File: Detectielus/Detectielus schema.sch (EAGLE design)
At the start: 12 parts, among them IC1 74HC132D, X1 Arduino

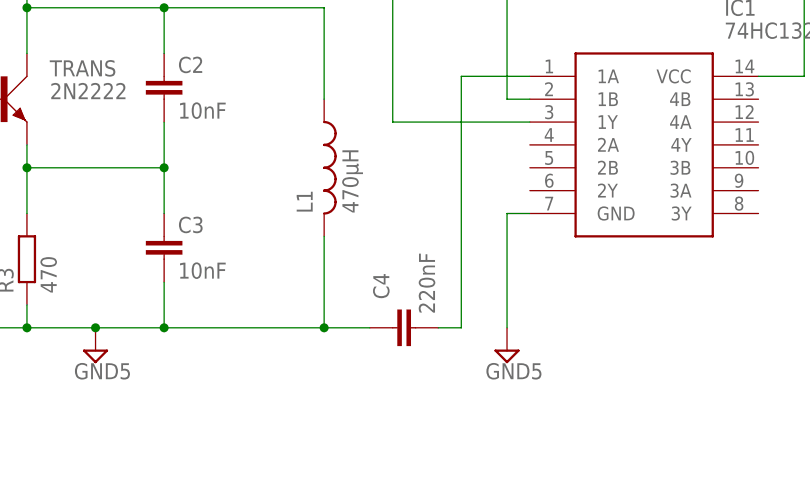
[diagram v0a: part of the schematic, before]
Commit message: Aanpassing schema (diode)
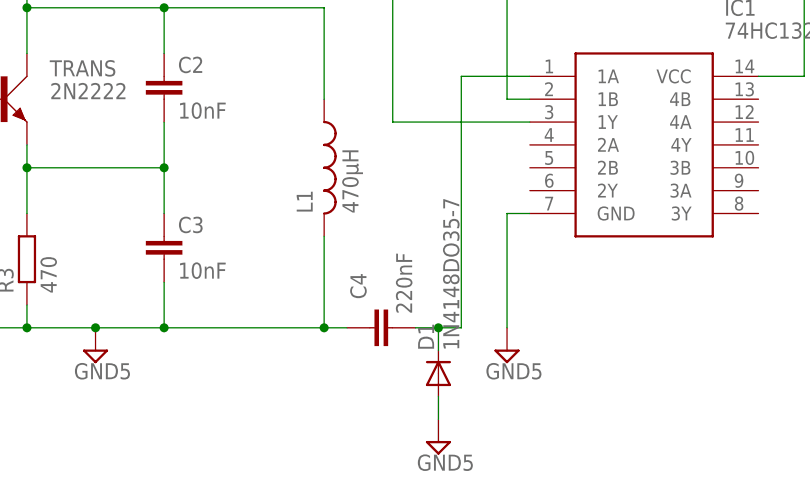
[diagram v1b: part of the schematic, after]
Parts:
- added D1: 1N4148DO35-7, Detectielus library:1N4148DO35-7
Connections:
- net GND5: now also D1.A
- net N$1: now also D1.C
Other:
- moved on the sheet: C4
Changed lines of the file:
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@@
 <layer number="97" name="Info" color="7" fill="1" visible="yes" active="yes"/>
 <layer number="98" name="Guide" color="6" fill="1" visible="yes" active="yes"/>
+<layer number="99" name="SpiceOrder" color="5" fill="1" visible="yes" active="yes"/>
 </layers>
 <schematic xreflabel="%F%N/%S.%C%R" xrefpart="/%S.%C%R">
@@
 <part name="SUPPLY4" library="Detectielus library" deviceset="GND5" device=""/>
 <part name="X1" library="Detectielus library" deviceset="332-02" device="" package3d_urn="urn:adsk.eagle:package:6810/1" value="Arduino"/>
+<part name="SUPPLY5" library="Detectielus library" deviceset="GND5" device=""/>
+<part name="D1" library="Detectielus library" deviceset="1N4148" device="DO35-7" package3d_urn="urn:adsk.eagle:package:43339/1"/>
 </parts>
 <sheets>
@@
 <attribute name="VALUE" x="16.764" y="28.321" size="1.778" layer="96"/>
 </instance>
-<instance part="C4" gate="G$1" x="40.64" y="22.86" smashed="yes" rot="R90">
-<attribute name="NAME" x="38.481" y="28.956" size="1.778" layer="95" rot="R270"/>
-<attribute name="VALUE" x="45.339" y="24.384" size="1.778" layer="96" rot="R90"/>
+<instance part="C4" gate="G$1" x="38.1" y="22.86" smashed="yes" rot="R90">
+<attribute name="NAME" x="35.941" y="28.956" size="1.778" layer="95" rot="R270"/>
+<attribute name="VALUE" x="42.799" y="24.384" size="1.778" layer="96" rot="R90"/>
 </instance>
 <instance part="L1" gate="G$1" x="33.02" y="40.64" smashed="yes">
@@
 <attribute name="NAME" x="41.402" y="73.66" size="1.524" layer="95" rot="R90"/>
 <attribute name="VALUE" x="39.243" y="70.358" size="1.778" layer="96" rot="R90"/>
+</instance>
+<instance part="SUPPLY5" gate="G$1" x="45.72" y="10.16" smashed="yes">
+<attribute name="VALUE" x="43.307" y="6.985" size="1.778" layer="96"/>
+</instance>
+<instance part="D1" gate="G$1" x="45.72" y="17.78" smashed="yes" rot="R90">
+<attribute name="NAME" x="45.2374" y="20.32" size="1.778" layer="95" rot="R90"/>
+<attribute name="VALUE" x="48.0314" y="20.32" size="1.778" layer="96" rot="R90"/>
 </instance>
 </instances>
@@
 <segment>
 <pinref part="C4" gate="G$1" pin="2"/>
+<wire x1="43.18" y1="22.86" x2="45.72" y2="22.86" width="0.1524" layer="91"/>
+<pinref part="IC1" gate="G$1" pin="1A"/>
 <wire x1="45.72" y1="22.86" x2="48.26" y2="22.86" width="0.1524" layer="91"/>
-<pinref part="IC1" gate="G$1" pin="1A"/>
 <wire x1="48.26" y1="22.86" x2="48.26" y2="50.8" width="0.1524" layer="91"/>
 <wire x1="48.26" y1="50.8" x2="55.88" y2="50.8" width="0.1524" layer="91"/>
+<wire x1="45.72" y1="20.32" x2="45.72" y2="22.86" width="0.1524" layer="91"/>
+<junction x="45.72" y="22.86"/>
+<pinref part="D1" gate="G$1" pin="C"/>
 </segment>
 </net>
@@
 <junction x="15.24" y="22.86"/>
 <pinref part="C4" gate="G$1" pin="1"/>
-<wire x1="38.1" y1="22.86" x2="33.02" y2="22.86" width="0.1524" layer="91"/>
+<wire x1="35.56" y1="22.86" x2="33.02" y2="22.86" width="0.1524" layer="91"/>
 <junction x="33.02" y="22.86"/>
 <pinref part="SUPPLY4" gate="G$1" pin="GND5"/>
@@
 <junction x="-15.24" y="22.86"/>
 </segment>
-</net>
+<segment>
+<pinref part="SUPPLY5" gate="G$1" pin="GND5"/>
+<wire x1="45.72" y1="12.7" x2="45.72" y2="15.24" width="0.1524" layer="91"/>
+<pinref part="D1" gate="G$1" pin="A"/>
+</segment>
+</net>

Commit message: Schema's en logboek
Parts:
- added X2, X3: (no value), Detectielus library:90-2
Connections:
- removed net VCC: IC1.1B, IC1.VCC, R1.2, R2.2
- new net GND: X2.1, X3.1
- new net VCC-24V: R1.2, R2.2, X2.2
- new net VCC-5V: IC1.1B, IC1.VCC, X3.2
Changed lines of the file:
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@@
 <setting verticaltext="up"/>
 </settings>
-<grid distance="0.1" unitdist="inch" unit="inch" style="lines" multiple="1" display="yes" altdistance="0.01" altunitdist="inch" altunit="inch"/>
+<grid distance="0.1" unitdist="inch" unit="inch" style="lines" multiple="1" display="no" altdistance="0.01" altunitdist="inch" altunit="inch"/>
 <layers>
 <layer number="1" name="Top" color="4" fill="1" visible="no" active="no"/>
@@
 <part name="SUPPLY3" library="Detectielus library" deviceset="GND5" device=""/>
 <part name="SUPPLY4" library="Detectielus library" deviceset="GND5" device=""/>
+<part name="D1" library="Detectielus library" deviceset="1N4148" device="DO35-7" package3d_urn="urn:adsk.eagle:package:43339/1"/>
 <part name="X1" library="Detectielus library" deviceset="332-02" device="" package3d_urn="urn:adsk.eagle:package:6810/1" value="Arduino"/>
 <part name="SUPPLY5" library="Detectielus library" deviceset="GND5" device=""/>
-<part name="D1" library="Detectielus library" deviceset="1N4148" device="DO35-7" package3d_urn="urn:adsk.eagle:package:43339/1"/>
+<part name="X2" library="Detectielus library" deviceset="90-2" device="" package3d_urn="urn:adsk.eagle:package:11443/1"/>
+<part name="X3" library="Detectielus library" deviceset="90-2" device="" package3d_urn="urn:adsk.eagle:package:11443/1"/>
 </parts>
 <sheets>
@@
 <attribute name="VALUE" x="5.207" y="17.145" size="1.778" layer="96"/>
 </instance>
+<instance part="D1" gate="G$1" x="45.72" y="17.78" smashed="yes" rot="R90">
+<attribute name="NAME" x="45.2374" y="20.32" size="1.778" layer="95" rot="R90"/>
+<attribute name="VALUE" x="48.0314" y="20.32" size="1.778" layer="96" rot="R90"/>
+</instance>
 <instance part="X1" gate="-1" x="40.64" y="71.12" smashed="yes" rot="R90">
 <attribute name="NAME" x="41.402" y="73.66" size="1.524" layer="95" rot="R90"/>
@@
 <attribute name="VALUE" x="43.307" y="6.985" size="1.778" layer="96"/>
 </instance>
-<instance part="D1" gate="G$1" x="45.72" y="17.78" smashed="yes" rot="R90">
-<attribute name="NAME" x="45.2374" y="20.32" size="1.778" layer="95" rot="R90"/>
-<attribute name="VALUE" x="48.0314" y="20.32" size="1.778" layer="96" rot="R90"/>
+<instance part="X2" gate="G$1" x="-66.04" y="78.74" smashed="yes" rot="R180">
+<attribute name="NAME" x="-66.04" y="76.962" size="1.778" layer="95" rot="R180"/>
+<attribute name="VALUE" x="-66.04" y="84.582" size="1.778" layer="96" rot="R180"/>
+</instance>
+<instance part="X3" gate="G$1" x="-66.04" y="68.58" smashed="yes" rot="R180">
+<attribute name="NAME" x="-66.04" y="66.802" size="1.778" layer="95" rot="R180"/>
+<attribute name="VALUE" x="-66.04" y="74.422" size="1.778" layer="96" rot="R180"/>
 </instance>
 </instances>
@@
 </segment>
 </net>
-<net name="VCC" class="0">
-<segment>
-<pinref part="R1" gate="G$1" pin="2"/>
-<wire x1="-15.24" y1="71.12" x2="-15.24" y2="73.66" width="0.1524" layer="91"/>
-<wire x1="-15.24" y1="73.66" x2="-7.62" y2="73.66" width="0.1524" layer="91"/>
-<pinref part="SUPPLY1" gate="G$1" pin="VCC"/>
-<wire x1="-7.62" y1="73.66" x2="-7.62" y2="76.2" width="0.1524" layer="91"/>
-<pinref part="R2" gate="G$1" pin="2"/>
-<wire x1="0" y1="71.12" x2="0" y2="73.66" width="0.1524" layer="91"/>
-<wire x1="0" y1="73.66" x2="-7.62" y2="73.66" width="0.1524" layer="91"/>
-<junction x="-7.62" y="73.66"/>
-</segment>
+<net name="VCC-5V" class="0">
 <segment>
 <pinref part="IC1" gate="G$1" pin="1B"/>
@@
 <wire x1="86.36" y1="60.96" x2="53.34" y2="60.96" width="0.1524" layer="91"/>
 <junction x="53.34" y="60.96"/>
+<label x="63.5" y="60.96" size="1.778" layer="95"/>
+</segment>
+<segment>
+<pinref part="X3" gate="G$1" pin="2"/>
+<wire x1="-63.5" y1="71.12" x2="-60.96" y2="71.12" width="0.1524" layer="91"/>
+<label x="-63.246" y="71.374" size="1.778" layer="95"/>
 </segment>
 </net>
@@
 </segment>
 <segment>
+<pinref part="D1" gate="G$1" pin="A"/>
+<wire x1="45.72" y1="15.24" x2="45.72" y2="12.7" width="0.1524" layer="91"/>
 <pinref part="SUPPLY5" gate="G$1" pin="GND5"/>
-<wire x1="45.72" y1="12.7" x2="45.72" y2="15.24" width="0.1524" layer="91"/>
-<pinref part="D1" gate="G$1" pin="A"/>
-</segment>
-</net>
+</segment>
+</net>
+<net name="VCC-24V" class="0">
+<segment>
+<pinref part="R1" gate="G$1" pin="2"/>
+<wire x1="-15.24" y1="71.12" x2="-15.24" y2="73.66" width="0.1524" layer="91"/>
+<wire x1="-15.24" y1="73.66" x2="-7.62" y2="73.66" width="0.1524" layer="91"/>
+<pinref part="SUPPLY1" gate="G$1" pin="VCC"/>
+<wire x1="-7.62" y1="73.66" x2="-7.62" y2="76.2" width="0.1524" layer="91"/>
+<pinref part="R2" gate="G$1" pin="2"/>
+<wire x1="0" y1="71.12" x2="0" y2="73.66" width="0.1524" layer="91"/>
+<wire x1="0" y1="73.66" x2="-7.62" y2="73.66" width="0.1524" layer="91"/>
+<junction x="-7.62" y="73.66"/>
+<label x="-12.7" y="73.66" size="1.778" layer="95"/>
+</segment>
+<segment>
+<pinref part="X2" gate="G$1" pin="2"/>
+<wire x1="-63.5" y1="81.28" x2="-60.96" y2="81.28" width="0.1524" layer="91"/>
+<label x="-63.246" y="81.534" size="1.778" layer="95"/>
+</segment>
+</net>
+<net name="GND" class="0">
+<segment>
+<pinref part="X2" gate="G$1" pin="1"/>
+<wire x1="-63.5" y1="78.74" x2="-60.96" y2="78.74" width="0.1524" layer="91"/>
+<label x="-63.246" y="78.994" size="1.778" layer="95"/>
+</segment>
+<segment>
+<pinref part="X3" gate="G$1" pin="1"/>
+<wire x1="-63.5" y1="68.58" x2="-60.96" y2="68.58" width="0.1524" layer="91"/>
+<label x="-63.246" y="68.834" size="1.778" layer="95"/>
+</segment>
+</net>
